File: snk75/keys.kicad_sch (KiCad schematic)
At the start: 255 parts

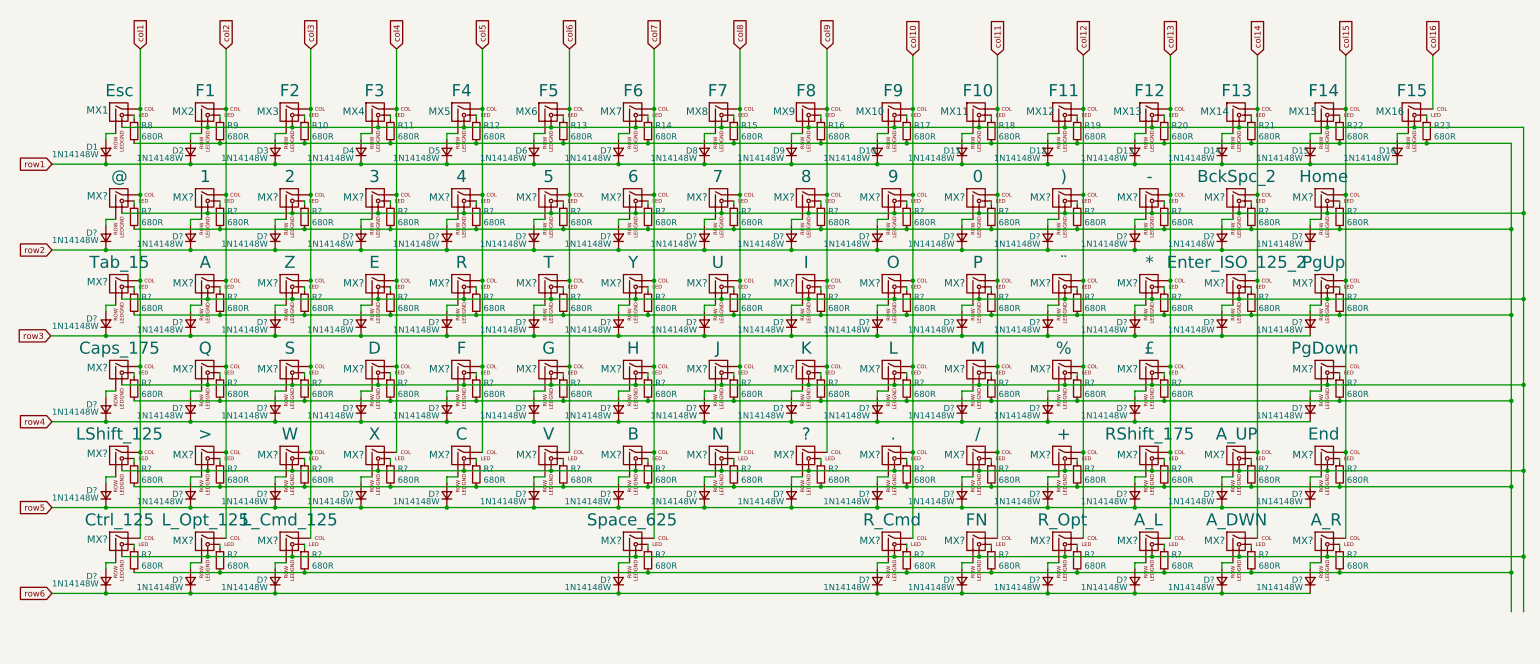
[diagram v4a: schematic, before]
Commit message: Added footprints for units more than 1
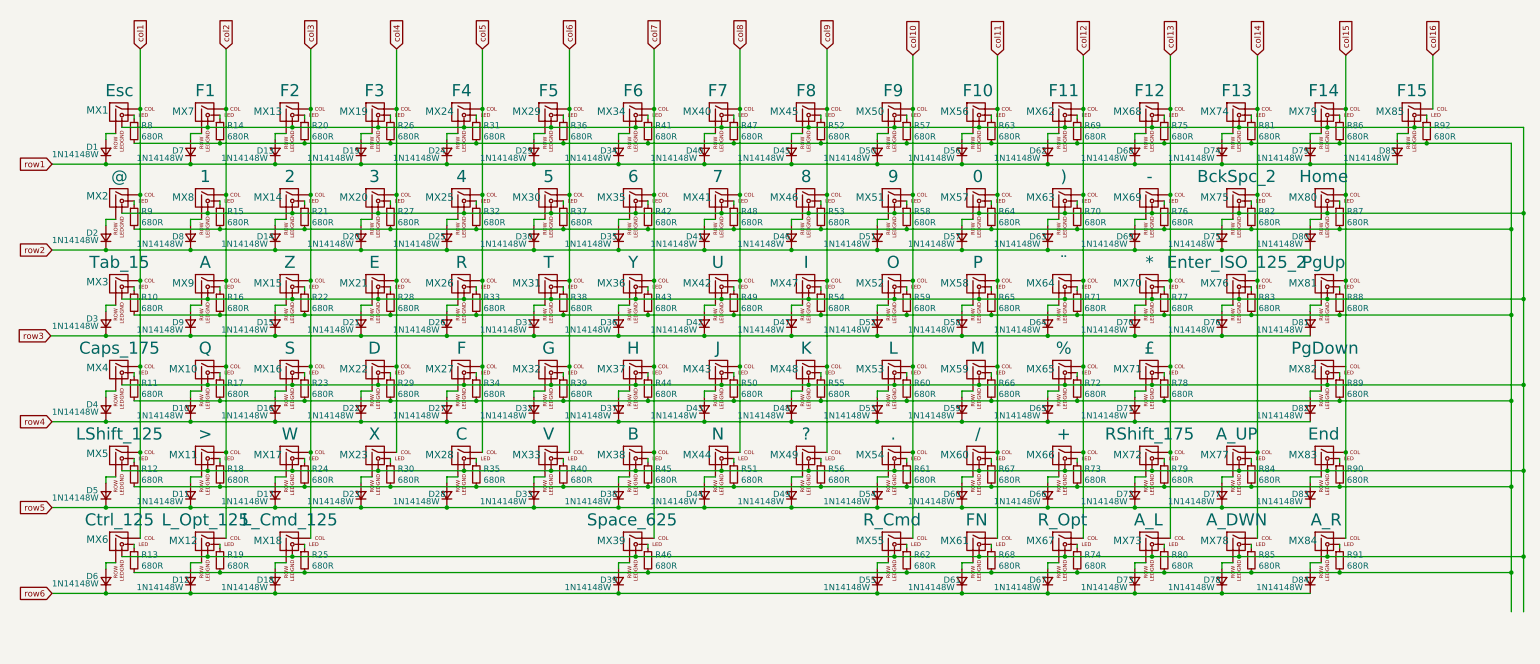
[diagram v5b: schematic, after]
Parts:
- MX12, MX18, MX5, MX6: renamed from MX?; footprint MX_Only:MXOnly-1U -> MX_Only:MXOnly-1.25U
- MX3: renamed from MX?; footprint MX_Only:MXOnly-1U -> MX_Only:MXOnly-1.5U
- MX39: renamed from MX?; footprint MX_Only:MXOnly-1U -> MX_Only:MXOnly-6.25U
- MX4, MX72: renamed from MX?; footprint MX_Only:MXOnly-1U -> MX_Only:MXOnly-1.75U
- MX75: renamed from MX?; footprint MX_Only:MXOnly-1U -> MX_Only:MXOnly-2U
- MX76: renamed from MX?; footprint MX_Only:MXOnly-1U -> MX_Only:MXOnly-ISO
- gave numbers to parts that had none: 197
- renumbered D3 to D13, D4 to D19, D5 to D24, D6 to D29, D7 to D34, D8 to D40, D9 to D45, D10 to D50, D11 to D56, D12 to D62, D13 to D68, D2 to D7, D14 to D74, D15 to D79, D16 to D85, MX3 to MX13, MX4 to MX19, MX5 to MX24, MX6 to MX29, MX7 to MX34, MX8 to MX40, MX9 to MX45, MX10 to MX50, MX11 to MX56, MX12 to MX62, MX13 to MX68, MX2 to MX7, MX14 to MX74, MX15 to MX79, MX16 to MX85, R9 to R14, R10 to R20, R11 to R26, R12 to R31, R13 to R36, R14 to R41, R15 to R47, R16 to R52, R17 to R57, R18 to R63, R19 to R69, R20 to R75, R21 to R81, R22 to R86, R23 to R92

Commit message: Began PCB design
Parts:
- MX1, MX10, MX11, MX13, MX14, MX15, MX16, MX17, MX19, MX2, MX20, MX21, MX22, MX23, MX24, MX25, MX26, MX27, MX28, MX29, MX30, MX31, MX32, MX33, MX34, MX35, MX36, MX37, MX38, MX40, MX41, MX42, MX43, MX44, MX45, MX46, MX47, MX48, MX49, MX50, MX51, MX52, MX53, MX54, MX55, MX56, MX57, MX58, MX59, MX60, MX61, MX62, MX63, MX64, MX65, MX66, MX67, MX68, MX69, MX7, MX70, MX71, MX73, MX74, MX77, MX78, MX79, MX8, MX80, MX81, MX82, MX83, MX84, MX85, MX9: footprint MX_Only:MXOnly-1U -> MX_Only:MXOnly-1U-FLIPPED
- MX12, MX18, MX5, MX6: footprint MX_Only:MXOnly-1.25U -> MX_Only:MXOnly-1.25U-FLIPPED
- MX3: footprint MX_Only:MXOnly-1.5U -> MX_Only:MXOnly-1.5U-FLIPPED
- MX39: footprint MX_Only:MXOnly-6.25U -> MX_Only:MXOnly-6.25U-FLIPPED
- MX4, MX72: footprint MX_Only:MXOnly-1.75U -> MX_Only:MXOnly-1.75U-FLIPPED
- MX75: footprint MX_Only:MXOnly-2U -> MX_Only:MXOnly-2U-FLIPPED

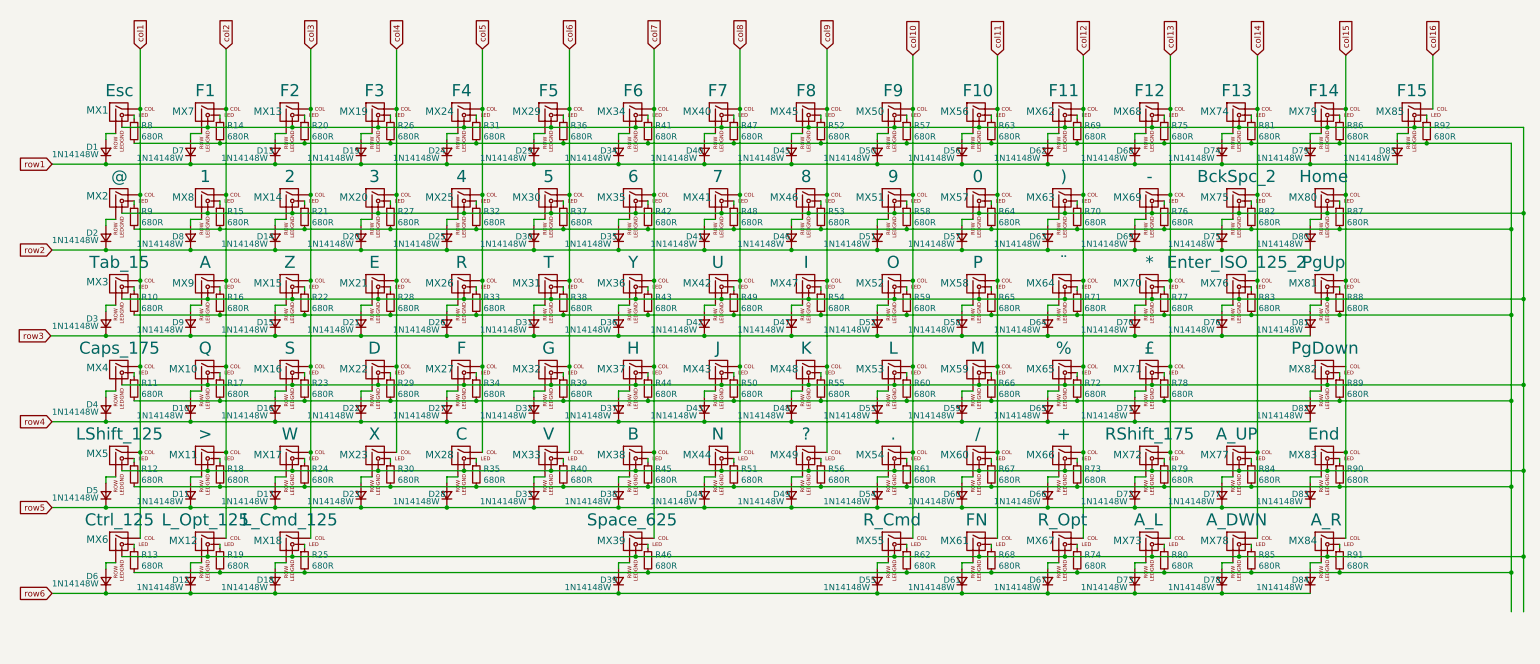
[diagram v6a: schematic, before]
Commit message: Fixed reset
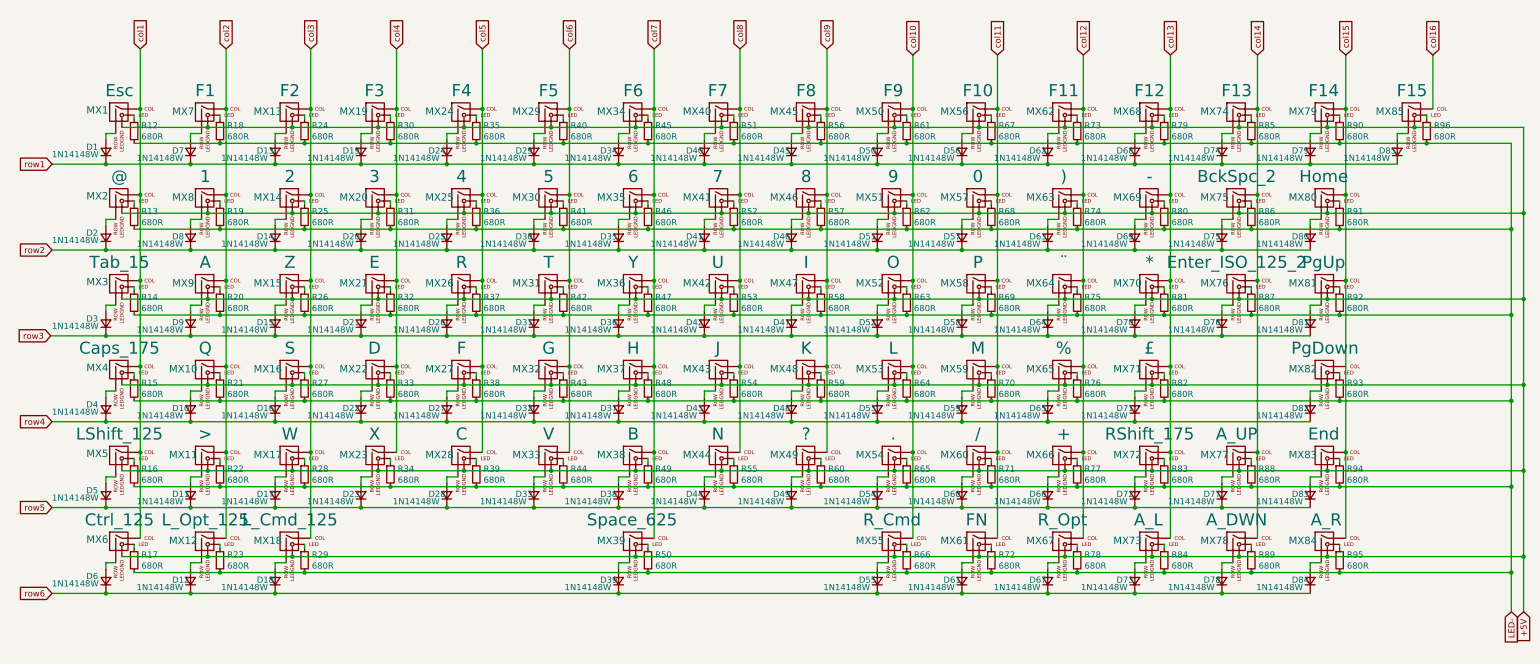
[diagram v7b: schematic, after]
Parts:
- MX1, MX10, MX11, MX13, MX14, MX15, MX16, MX17, MX19, MX2, MX20, MX21, MX22, MX23, MX24, MX25, MX26, MX27, MX28, MX29, MX30, MX31, MX32, MX33, MX34, MX35, MX36, MX37, MX38, MX40, MX41, MX42, MX43, MX44, MX45, MX46, MX47, MX48, MX49, MX50, MX51, MX52, MX53, MX54, MX55, MX56, MX57, MX58, MX59, MX60, MX61, MX62, MX63, MX64, MX65, MX66, MX67, MX68, MX69, MX7, MX70, MX71, MX73, MX74, MX77, MX78, MX79, MX8, MX80, MX81, MX82, MX83, MX84, MX85, MX9: footprint MX_Only:MXOnly-1U-FLIPPED -> MX_Only:MXOnly-1U
- MX12, MX18, MX5, MX6: footprint MX_Only:MXOnly-1.25U-FLIPPED -> MX_Only:MXOnly-1.25U
- MX3: footprint MX_Only:MXOnly-1.5U-FLIPPED -> MX_Only:MXOnly-1.5U
- MX39: footprint MX_Only:MXOnly-6.25U-FLIPPED -> MX_Only:MXOnly-6.25U
- MX4, MX72: footprint MX_Only:MXOnly-1.75U-FLIPPED -> MX_Only:MXOnly-1.75U
- MX75: footprint MX_Only:MXOnly-2U-FLIPPED -> MX_Only:MXOnly-2U
- renumbered R8 to R12, R9 to R13, R10 to R14, R11 to R15, R12 to R16, R13 to R17, R14 to R18, R15 to R19, R16 to R20, R17 to R21, R18 to R22, R19 to R23, R20 to R24, R21 to R25, R22 to R26, R23 to R27, R24 to R28, R25 to R29, R26 to R30, R27 to R31, R28 to R32, R29 to R33, R30 to R34, R31 to R35, R32 to R36, R33 to R37, R34 to R38, R35 to R39, R36 to R40, R37 to R41, R38 to R42, R39 to R43, R40 to R44, R41 to R45, R42 to R46, R43 to R47, R44 to R48, R45 to R49, R46 to R50, R47 to R51, R48 to R52, R49 to R53, R50 to R54, R51 to R55, R52 to R56, R53 to R57, R54 to R58, R55 to R59, R56 to R60, R57 to R61, R58 to R62, R59 to R63, R60 to R64, R61 to R65, R62 to R66, R63 to R67, R64 to R68, R65 to R69, R66 to R70, R67 to R71, R68 to R72, R69 to R73, R70 to R74, R71 to R75, R72 to R76, R73 to R77, R74 to R78, R75 to R79, R76 to R80, R77 to R81, R78 to R82, R79 to R83, R80 to R84, R81 to R85, R82 to R86, R83 to R87, R84 to R88, R85 to R89, R86 to R90, R87 to R91, R88 to R92, R89 to R93, R90 to R94, R91 to R95, R92 to R96
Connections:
- net LED-: now reaches R12.2, R13.2, R14.2, R15.2, R16.2, R17.2, R18.2, R19.2, R20.2, R21.2, R22.2, R23.2, R24.2, R25.2, R26.2, R27.2, R28.2, R29.2, R30.2, R31.2, R32.2, R33.2, R34.2, R35.2, R36.2, R37.2, R38.2, R39.2, R40.2, R41.2, R42.2, R43.2, R44.2, R45.2, R46.2, R47.2, R48.2, R49.2, R50.2, R51.2, R52.2, R53.2, R54.2, R55.2, R56.2, R57.2, R58.2, R59.2, R60.2, R61.2, R62.2, R63.2, R64.2, R65.2, R66.2, R67.2, R68.2, R69.2, R70.2, R71.2, R72.2, R73.2, R74.2, R75.2, R76.2, R77.2, R78.2, R79.2, R80.2, R81.2, R82.2, R83.2, R84.2, R85.2, R86.2, R87.2, R88.2, R89.2, R90.2, R91.2, R92.2, R93.2, R94.2, R95.2, R96.2
- net +5V: now reaches MX1.4 (LEDGND), MX10.4 (LEDGND), MX11.4 (LEDGND), MX12.4 (LEDGND), MX13.4 (LEDGND), MX14.4 (LEDGND), MX15.4 (LEDGND), MX16.4 (LEDGND), MX17.4 (LEDGND), MX18.4 (LEDGND), MX19.4 (LEDGND), MX2.4 (LEDGND), MX20.4 (LEDGND), MX21.4 (LEDGND), MX22.4 (LEDGND), MX23.4 (LEDGND), MX24.4 (LEDGND), MX25.4 (LEDGND), MX26.4 (LEDGND), MX27.4 (LEDGND), MX28.4 (LEDGND), MX29.4 (LEDGND), MX3.4 (LEDGND), MX30.4 (LEDGND), MX31.4 (LEDGND), MX32.4 (LEDGND), MX33.4 (LEDGND), MX34.4 (LEDGND), MX35.4 (LEDGND), MX36.4 (LEDGND), MX37.4 (LEDGND), MX38.4 (LEDGND), MX39.4 (LEDGND), MX4.4 (LEDGND), MX40.4 (LEDGND), MX41.4 (LEDGND), MX42.4 (LEDGND), MX43.4 (LEDGND), MX44.4 (LEDGND), MX45.4 (LEDGND), MX46.4 (LEDGND), MX47.4 (LEDGND), MX48.4 (LEDGND), MX49.4 (LEDGND), MX5.4 (LEDGND), MX50.4 (LEDGND), MX51.4 (LEDGND), MX52.4 (LEDGND), MX53.4 (LEDGND), MX54.4 (LEDGND), MX55.4 (LEDGND), MX56.4 (LEDGND), MX57.4 (LEDGND), MX58.4 (LEDGND), MX59.4 (LEDGND), MX6.4 (LEDGND), MX60.4 (LEDGND), MX61.4 (LEDGND), MX62.4 (LEDGND), MX63.4 (LEDGND), MX64.4 (LEDGND), MX65.4 (LEDGND), MX66.4 (LEDGND), MX67.4 (LEDGND), MX68.4 (LEDGND), MX69.4 (LEDGND), MX7.4 (LEDGND), MX70.4 (LEDGND), MX71.4 (LEDGND), MX72.4 (LEDGND), MX73.4 (LEDGND), MX74.4 (LEDGND), MX75.4 (LEDGND), MX76.4 (LEDGND), MX77.4 (LEDGND), MX78.4 (LEDGND), MX79.4 (LEDGND), MX8.4 (LEDGND), MX80.4 (LEDGND), MX81.4 (LEDGND), MX82.4 (LEDGND), MX83.4 (LEDGND), MX84.4 (LEDGND), MX85.4 (LEDGND), MX9.4 (LEDGND)

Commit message: Fixed label
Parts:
- renumbered R12 to R10, R13 to R11, R14 to R12, R15 to R13, R16 to R14, R17 to R15, R18 to R16, R19 to R17, R20 to R18, R21 to R19, R22 to R20, R23 to R21, R24 to R22, R25 to R23, R26 to R24, R27 to R25, R28 to R26, R29 to R27, R30 to R28, R31 to R29, R32 to R30, R33 to R31, R34 to R32, R35 to R33, R36 to R34, R37 to R35, R38 to R36, R39 to R37, R40 to R38, R41 to R39, R42 to R40, R43 to R41, R44 to R42, R45 to R43, R46 to R44, R47 to R45, R48 to R46, R49 to R47, R50 to R48, R51 to R49, R52 to R50, R53 to R51, R54 to R52, R55 to R53, R56 to R54, R57 to R55, R58 to R56, R59 to R57, R60 to R58, R61 to R59, R62 to R60, R63 to R61, R64 to R62, R65 to R63, R66 to R64, R67 to R65, R68 to R66, R69 to R67, R70 to R68, R71 to R69, R72 to R70, R73 to R71, R74 to R72, R75 to R73, R76 to R74, R77 to R75, R78 to R76, R79 to R77, R80 to R78, R81 to R79, R82 to R80, R83 to R81, R84 to R82, R85 to R83, R86 to R84, R87 to R85, R88 to R86, R89 to R87, R90 to R88, R91 to R89, R92 to R90, R93 to R91, R94 to R92, R95 to R93, R96 to R94
